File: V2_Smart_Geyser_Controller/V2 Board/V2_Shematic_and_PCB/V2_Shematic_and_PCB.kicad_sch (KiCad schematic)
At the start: 1 part, among them J1 1714984

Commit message: Schematic update: AC-DC Converter added. TPS62903RPJR regulator circuit added. The circuit still annotation
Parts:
- added C1, C3: C, symbol Device:C
- added C2: 10uF, Capacitor_SMD:C_0805_2012Metric, symbol Device:C
- added K1: SLA-12VDC-SL-C, SLA-12VDC-SL-C:RELAY_SLA-12VDC-SL-C, symbol SLA-12VDC-SL-C:SLA-12VDC-SL-C
- added L1: L, symbol Device:L
- added R1, R2, R3: R, symbol Device:R
- added U1: IRM-15-12, footprintsIRM:IRM-15_MWU, symbol 2026-09-15_03-44-23:IRM-15-12
- added U3: TPS62903RPJR, RPJ0009A, symbol 2026-09-19_18-21-30:TPS62903RPJR
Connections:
- net MAINS_NEUTRAL: now reaches J1.1
- net MAINS_NEUTRAL: now also U1.4 (AC/L)
- net EARTH: now reaches J1.2
- net MAINS_LIVE: now reaches J1.3
- net MAINS_LIVE: now also U1.3 (AC/N)
- new net: L1.1, U3.2 (SW)
- new net: R1.2, U3.1 (PG)
- new net: K1.COM1, K1.COM2
- new net: C1.1, U3.8 (SS_TR)
- new net: R2.1, R3.2, U3.9 (FB_VSET)
- new net 12 V: C2.1, U1.2 (+V), U3.5 (EN), U3.6 (VIN)
- new net 3.3 V: C3.1, L1.2, R1.1, R2.2, U3.3 (VOS)
- new net GND: C1.2, C2.2, C3.2, R3.1, U1.1 (-V), U3.4 (GND), U3.7 (MODE_S-CONF)
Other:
- moved on the sheet: J1

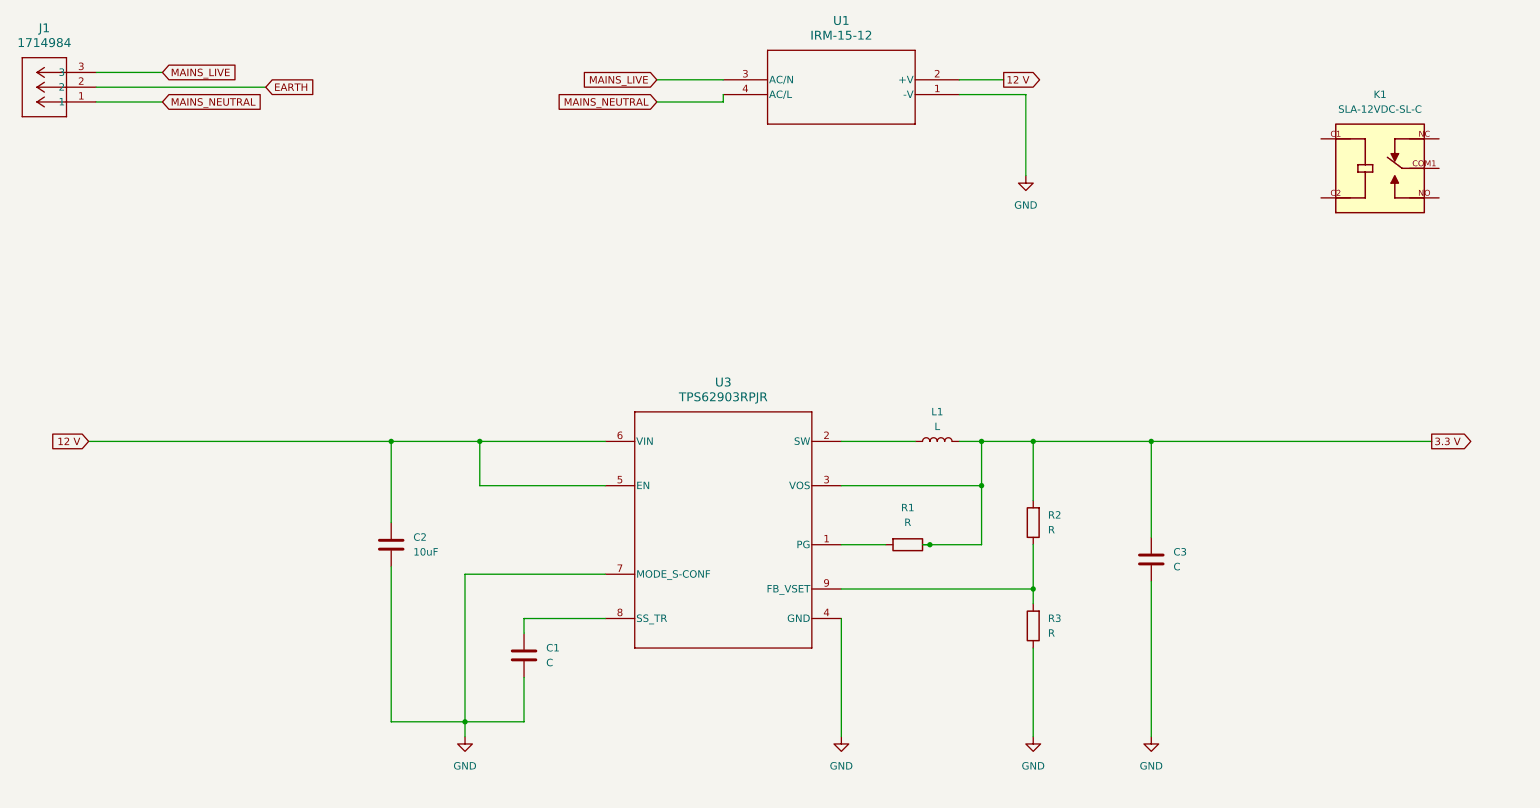
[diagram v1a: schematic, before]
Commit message: Annotated regulator PSU circuit
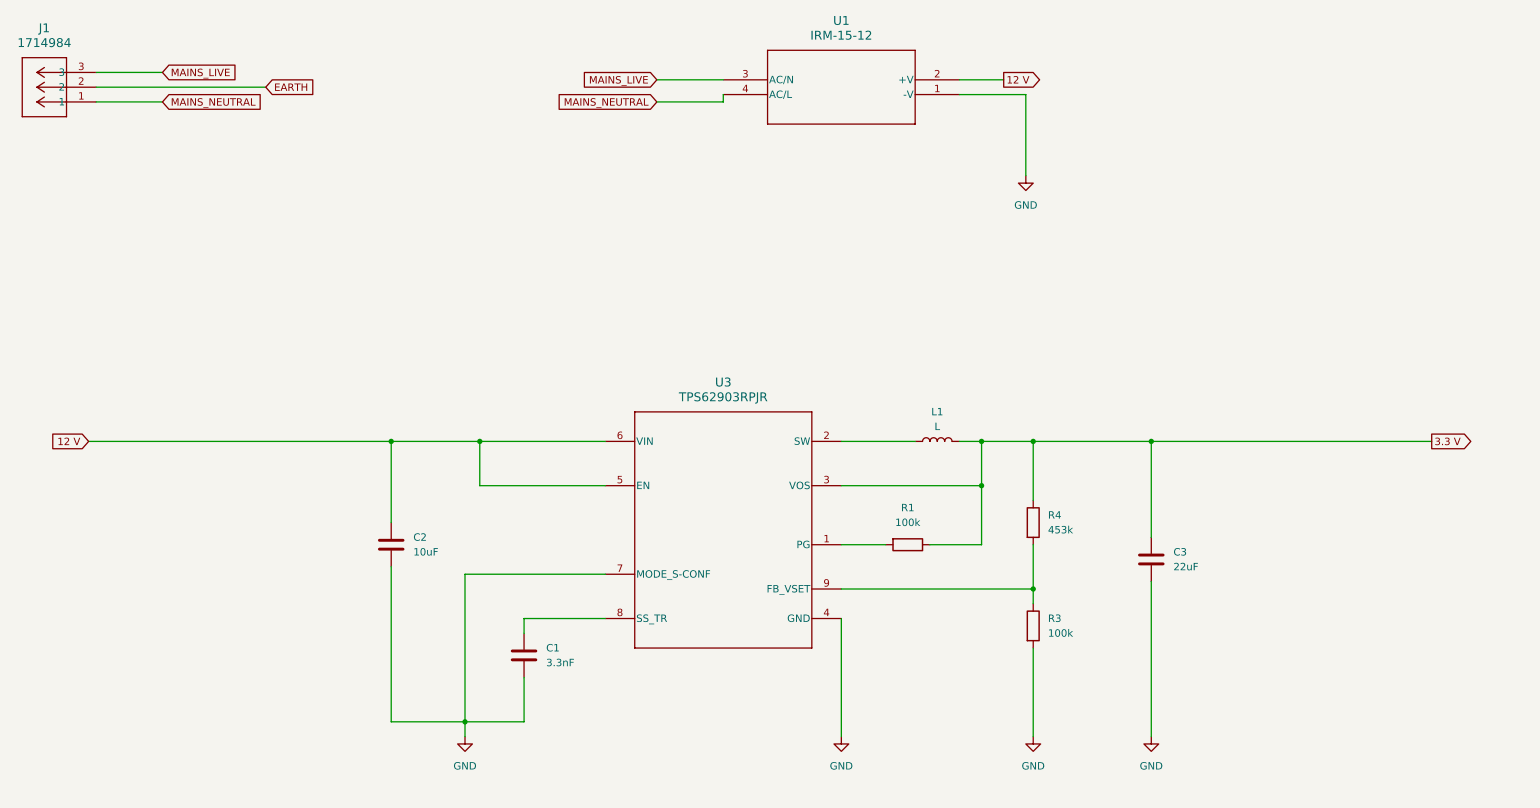
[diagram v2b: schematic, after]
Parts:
- removed K1: SLA-12VDC-SL-C, SLA-12VDC-SL-C:RELAY_SLA-12VDC-SL-C, symbol SLA-12VDC-SL-C:SLA-12VDC-SL-C
- removed R2: R, symbol Device:R
- added R4: 453k, Resistor_SMD:R_0805_2012Metric, symbol Device:R
- C1: value C -> 3.3nF; footprint (none) -> Capacitor_SMD:C_0603_1608Metric; LCSC Part # (none) -> C1613; MPN (none) -> LCSC Part #
- C2: LCSC Part # C2167423 -> C15850; MPN (none) -> CL21A106KAYNNNE
- C3: value C -> 22uF; footprint (none) -> Capacitor_SMD:C_0805_2012Metric; LCSC Part # (none) -> C3010429; MPN (none) -> GRT21BD70J226ME13L
- L1: footprint (none) -> footprintsInductor:IND_BOURNS_SRN8040; LCSC Part # (none) -> C2041438; MPN (none) -> SRN8040-1R0Y
- R1, R3: value R -> 100k; footprint (none) -> Resistor_SMD:R_0805_2012Metric; LCSC Part # (none) -> C2907217; MPN (none) -> FRC0805F1003TS
- U3: footprint RPJ0009A -> footprintsTPS62903RPJR:RPJ0009A; LCSC Part # (none) -> C2866502; MPN (none) -> TPS62903RPJR
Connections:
- net 3.3 V: now also R4.1
- net GND: now also R3.2; no longer R3.1
- net at U3.9 (FB_VSET): now also R3.1, R4.2; no longer R3.2

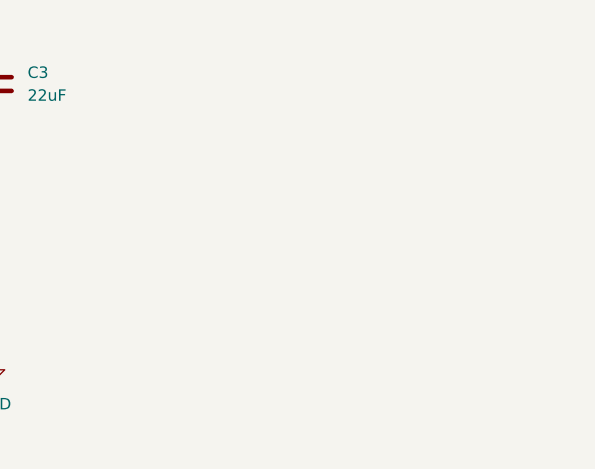
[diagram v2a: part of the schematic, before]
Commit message: Added relay and it drive circuit, still needs annotation
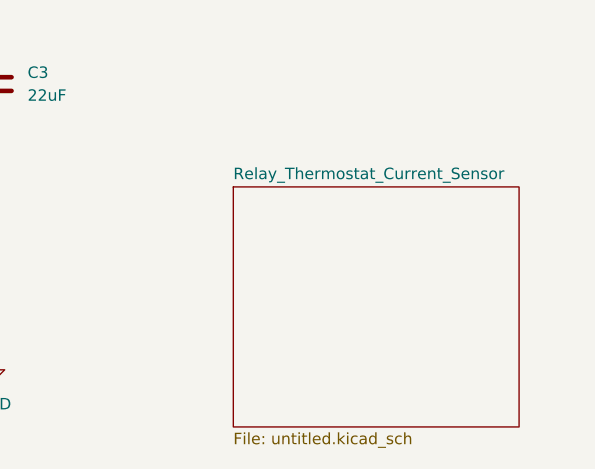
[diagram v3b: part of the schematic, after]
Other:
- added sheet Relay_Thermostat_Current_Sensor (untitled.kicad_sch)
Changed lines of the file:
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@@
+		)
+	)
+	(sheet
+		(at 240.03 123.19)
+		(size 31.75 26.67)
+		(exclude_from_sim no)
+		(in_bom yes)
+		(on_board yes)
+		(dnp no)
+		(fields_autoplaced yes)
+		(stroke
+			(width 0.1524)
+			(type solid)
+		)
+		(fill
+			(color 0 0 0 0)
+		)
+		(property "Sheetname" "Relay_Thermostat_Current_Sensor"
+			(at 240.03 122.4784 0)
+			(show_name no)
+			(do_not_autoplace no)
+			(effects
+				(font
+					(size 1.27 1.27)
+				)
+				(justify left bottom)
+			)
+		)
+		(property "Sheetfile" "untitled.kicad_sch"
+			(at 240.03 150.4446 0)
+			(show_name no)
+			(do_not_autoplace no)
+			(effects
+				(font
+					(size 1.27 1.27)
+				)
+				(justify left top)
+			)
+		)
+		(instances
+			(project "V2_Shematic_and_PCB"
+				(path "/ac98abae-ce0c-47cc-9f44-8efe46af5eb9"
+					(page "2")
+				)
+			)
 		)
 	)
